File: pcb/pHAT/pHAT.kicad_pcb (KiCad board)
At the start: 2 copper layers, 65 x 30 mm, 37 parts, among them M1 mount1, M2 mount1, M3 mount1, M4 mount1, P2 USB_A, P4 CONN_01X30, SW1 SW_Push, SW2 SW_Push, SW3 SW_Push, U1 ATTINY25/45/85

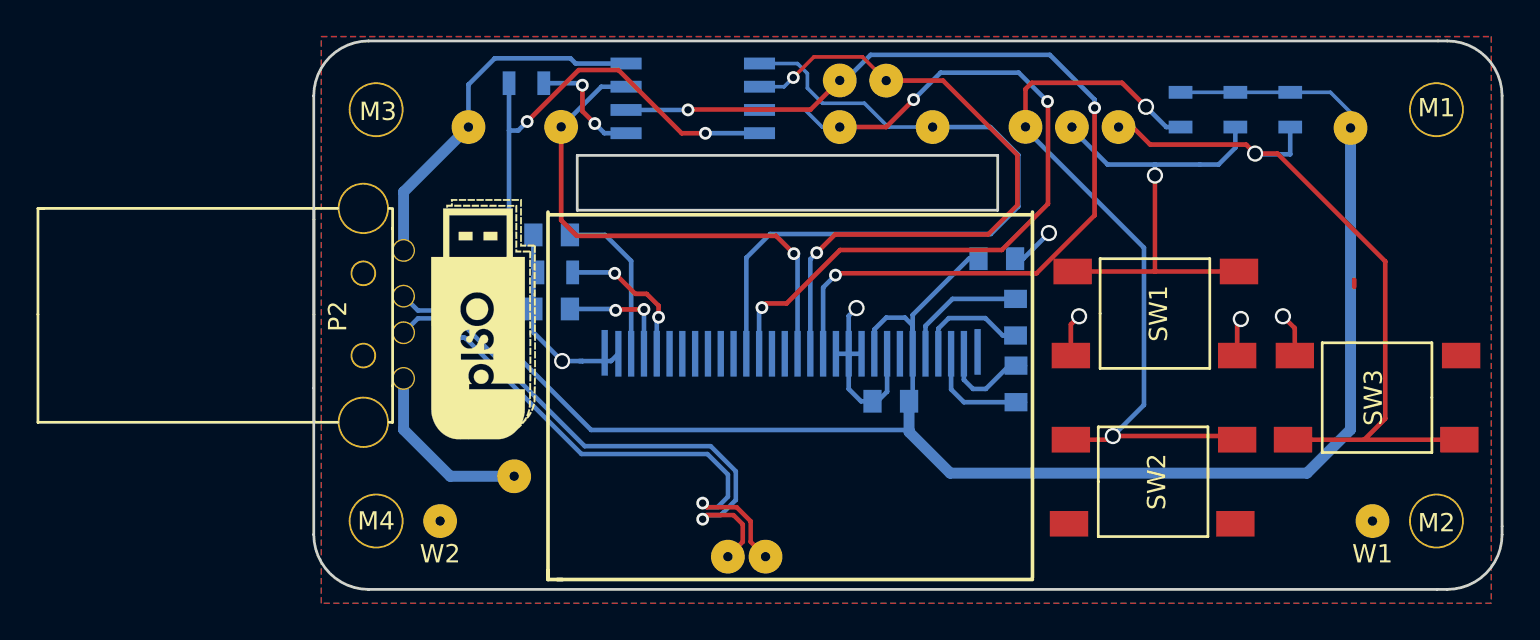
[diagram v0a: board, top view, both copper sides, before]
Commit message: update PCB for 1.2 support
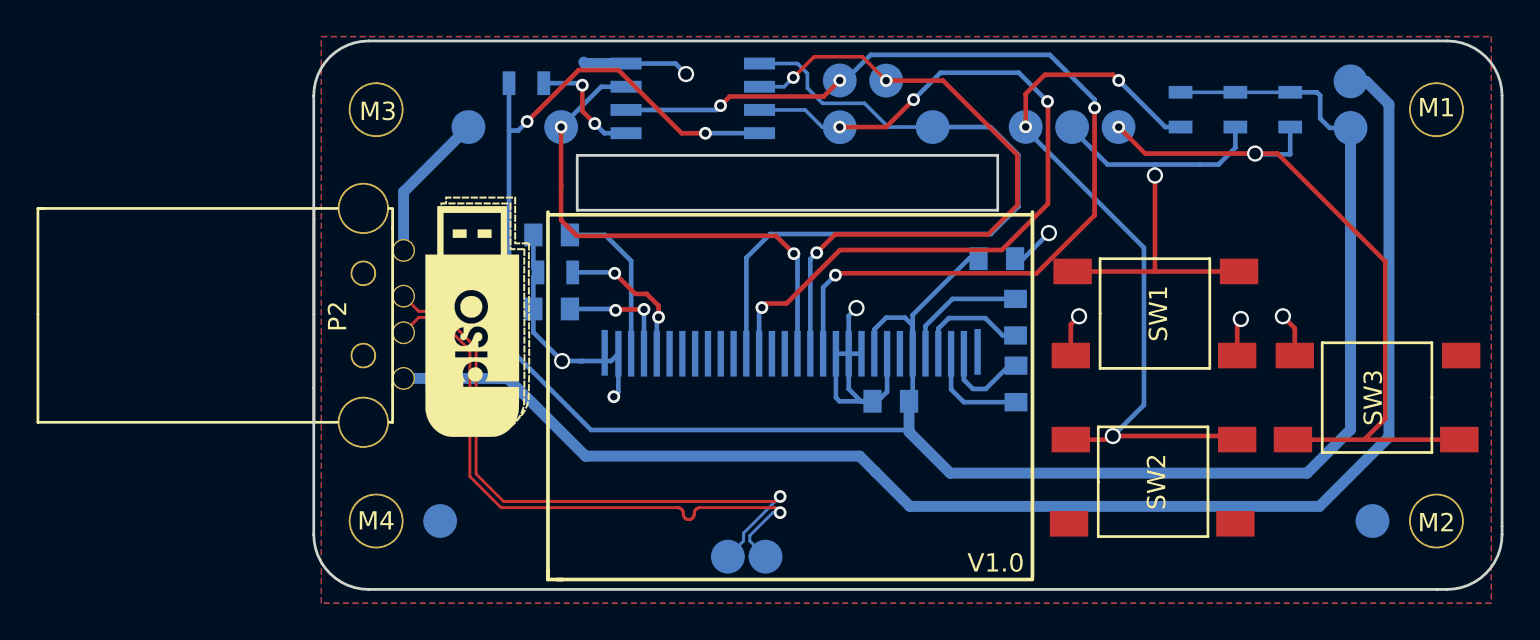
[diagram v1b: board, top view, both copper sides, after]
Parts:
- removed D+: D_P, pISO:SLP
- removed D-: D_N, pISO:SLP
- removed G***: LOGO, pISO:LOGO
- added DNP1: LOGO, pISO:LOGO, F.Cu at (118.5, 94.6)
- added REF***: OSHW-Logo_19x20mm_SilkScreen, Symbols:OSHW-Logo_19x20mm_SilkScreen, B.Cu at (158.7, 95.5)
- added W14: D_N, pISO:SLP, B.Cu at (134.2, 107.7)
- added W15: D_P, pISO:SLP, B.Cu at (132.2, 107.7)
- moved W5 50.6 mm to (166.2, 81.7)
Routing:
- net Net-(P2-Pad1): track 9.91 -> 79.2 mm
- net /DM1_N: track 30.6 -> 34.7 mm
- net /DM1_P: track 30.6 -> 34.7 mm
- net GND: track 52.9 -> 54.1 mm, vias 6 -> 8
- net +3V3: track 124.7 -> 125.8 mm
- net Net-(A1-Pad1): track 42.5 -> 41.7 mm, vias 2 -> 3
- net /CS: vias 3 -> 4
- net /SCLK: vias 3 -> 4
- net /DC: vias 1 -> 2
- net Net-(B1-Pad1): vias 1 -> 2
- net /RST: vias 2 -> 3
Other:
- board text added: "+"
- board text added: "-"
- board text added: "V1.0"

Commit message: update PCB images
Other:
- board text added: "DOWN"
- board text added: "SELECT"
- board text added: "UP"
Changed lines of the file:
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@@
     (area 109.424999 79.424999 174.575001 109.575001)
     (thickness 1.6)
-    (drawings 25)
+    (drawings 28)
     (tracks 333)
     (zones 0)
@@
     (35 F.Paste user)
     (36 B.SilkS user)
-    (37 F.SilkS user hide)
+    (37 F.SilkS user)
     (38 B.Mask user)
     (39 F.Mask user)
@@
   )
   (setup
-    (last_trace_width 0.254)
+    (last_trace_width 0.2)
     (user_trace_width 0.2)
     (user_trace_width 0.25)
@@
   (module pISO:SLP (layer F.Cu)
     (at 167.41188 105.75942)
-    (fp_text reference W1 (at 0.04 5.3) (layer F.SilkS) hide
+    (fp_text reference W1 (at 11.5 -24.5) (layer F.SilkS) hide
       (effects (font (size 1 1) (thickness 0.15)))
     )
@@
   (module pISO:SLP (layer F.Cu)
     (at 116.41188 105.75942)
-    (fp_text reference W2 (at 0.01 5.31) (layer F.SilkS) hide
+    (fp_text reference W2 (at 62.5 -18.5) (layer F.SilkS) hide
       (effects (font (size 1 1) (thickness 0.15)))
     )
@@
   (module pISO:SLP (layer B.Cu)
     (at 134.21188 107.70942)
-    (fp_text reference W14 (at 0.2 3.47) (layer B.SilkS) hide
+    (fp_text reference W14 (at 44.7 -22.45) (layer B.SilkS) hide
       (effects (font (size 1 1) (thickness 0.15)) (justify mirror))
     )
@@
   (module pISO:SLP (layer B.Cu)
     (at 132.15188 107.70942)
-    (fp_text reference W15 (at -0.77 3.65) (layer B.SilkS) hide
+    (fp_text reference W15 (at 46.76 -21.45) (layer B.SilkS) hide
       (effects (font (size 1 1) (thickness 0.15)) (justify mirror))
     )
@@
   (module pISO:SLP (layer B.Cu)
     (at 148.44188 84.19942)
-    (fp_text reference A1 (at 0.13 -5.8) (layer B.SilkS) hide
+    (fp_text reference A1 (at 30.47 0.06) (layer B.SilkS) hide
       (effects (font (size 1 1) (thickness 0.15)) (justify mirror))
     )
@@
   (module pISO:SLP (layer B.Cu)
     (at 153.52188 84.20942)
-    (fp_text reference B1 (at 0.14 -5.71) (layer B.SilkS) hide
+    (fp_text reference B1 (at 25.39 -0.95) (layer B.SilkS) hide
       (effects (font (size 1 1) (thickness 0.15)) (justify mirror))
     )
@@
   (module pISO:SLP (layer B.Cu)
     (at 150.98188 84.20942)
-    (fp_text reference NO1 (at 0.17 -6.2) (layer B.SilkS) hide
+    (fp_text reference NO1 (at 27.93 -1.95) (layer B.SilkS) hide
       (effects (font (size 1 1) (thickness 0.15)) (justify mirror))
     )
@@
   (module pISO:SLP (layer B.Cu)
     (at 166.21188 81.70942)
-    (fp_text reference W5 (at 0.03 -4.9) (layer B.SilkS) hide
+    (fp_text reference W5 (at 12.7 -2.45) (layer B.SilkS) hide
       (effects (font (size 1 1) (thickness 0.15)) (justify mirror))
     )
@@
   (module pISO:SLP (layer B.Cu)
     (at 140.81188 81.66942)
-    (fp_text reference W7 (at 0.01 -5.09) (layer B.SilkS) hide
+    (fp_text reference W7 (at 38.1 7.59) (layer B.SilkS) hide
       (effects (font (size 1 1) (thickness 0.15)) (justify mirror))
     )
@@
   (module pISO:SLP (layer B.Cu)
     (at 138.27188 81.65942)
-    (fp_text reference W8 (at 0.31 -5.52) (layer B.SilkS) hide
+    (fp_text reference W8 (at 40.64 9.6) (layer B.SilkS) hide
       (effects (font (size 1 1) (thickness 0.15)) (justify mirror))
     )
@@
   (module pISO:SLP (layer B.Cu)
     (at 143.35188 84.20942)
-    (fp_text reference W9 (at -0.22 -6.82) (layer B.SilkS) hide
+    (fp_text reference W9 (at 35.56 4.05) (layer B.SilkS) hide
       (effects (font (size 1 1) (thickness 0.15)) (justify mirror))
     )
@@
   (module pISO:SLP (layer B.Cu)
     (at 138.27188 84.21942)
-    (fp_text reference W10 (at 0.17 -6.35) (layer B.SilkS) hide
+    (fp_text reference W10 (at 40.64 6.04) (layer B.SilkS) hide
       (effects (font (size 1 1) (thickness 0.15)) (justify mirror))
     )
@@
   (module pISO:SLP (layer B.Cu)
     (at 123.03188 84.20942)
-    (fp_text reference W11 (at 0 -6.64) (layer B.SilkS) hide
+    (fp_text reference W11 (at 55.88 8.05) (layer B.SilkS) hide
       (effects (font (size 1 1) (thickness 0.15)) (justify mirror))
     )
@@
   (module pISO:SLP (layer B.Cu)
     (at 117.96188 84.20942)
-    (fp_text reference W12 (at 0.33 -6.99) (layer B.SilkS) hide
+    (fp_text reference W12 (at 60.95 9.05) (layer B.SilkS) hide
       (effects (font (size 1 1) (thickness 0.15)) (justify mirror))
     )
@@
   (module pISO:SLP (layer B.Cu)
     (at 166.21188 84.25942)
-    (fp_text reference W13 (at 0.03 -5.69) (layer B.SilkS) hide
+    (fp_text reference W13 (at 12.7 -4) (layer B.SilkS) hide
       (effects (font (size 1 1) (thickness 0.15)) (justify mirror))
     )
@@
       (xy 1.060052 9.972623) (xy 1.248305 8.97404)) (layer B.SilkS) (width 0.01))
   )
+  (gr_text SELECT (at 167.71188 95.25942) (layer F.SilkS)
+    (effects (font (size 1 1) (thickness 0.25)))
+  )
+  (gr_text DOWN (at 155.21188 99.85942) (layer F.SilkS)
+    (effects (font (size 1 1) (thickness 0.25)))
+  )
+  (gr_text UP (at 155.41188 90.65942) (layer F.SilkS)
+    (effects (font (size 1 1) (thickness 0.25)))
+  )
   (gr_text V1.0 (at 146.81188 108.05942) (layer F.SilkS)

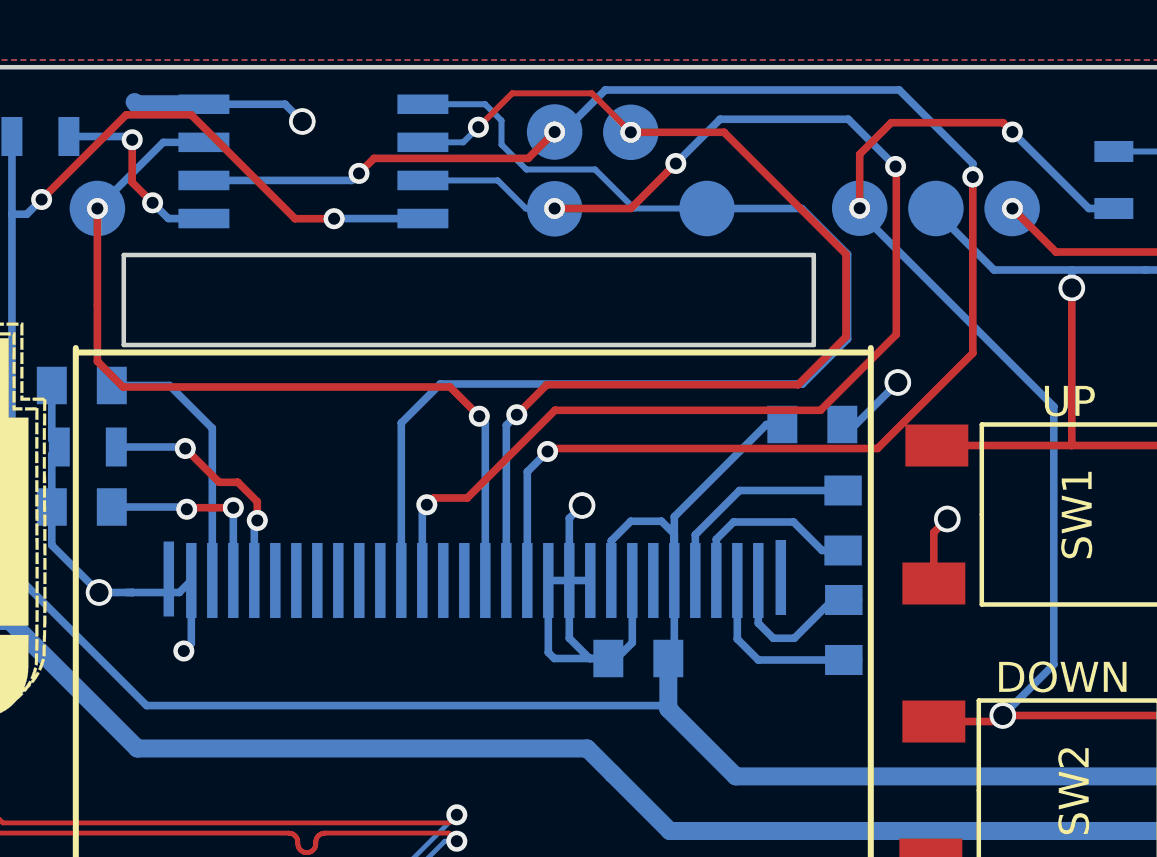
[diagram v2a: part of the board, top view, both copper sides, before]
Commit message: fixed issue that could cause CS line to short to up button
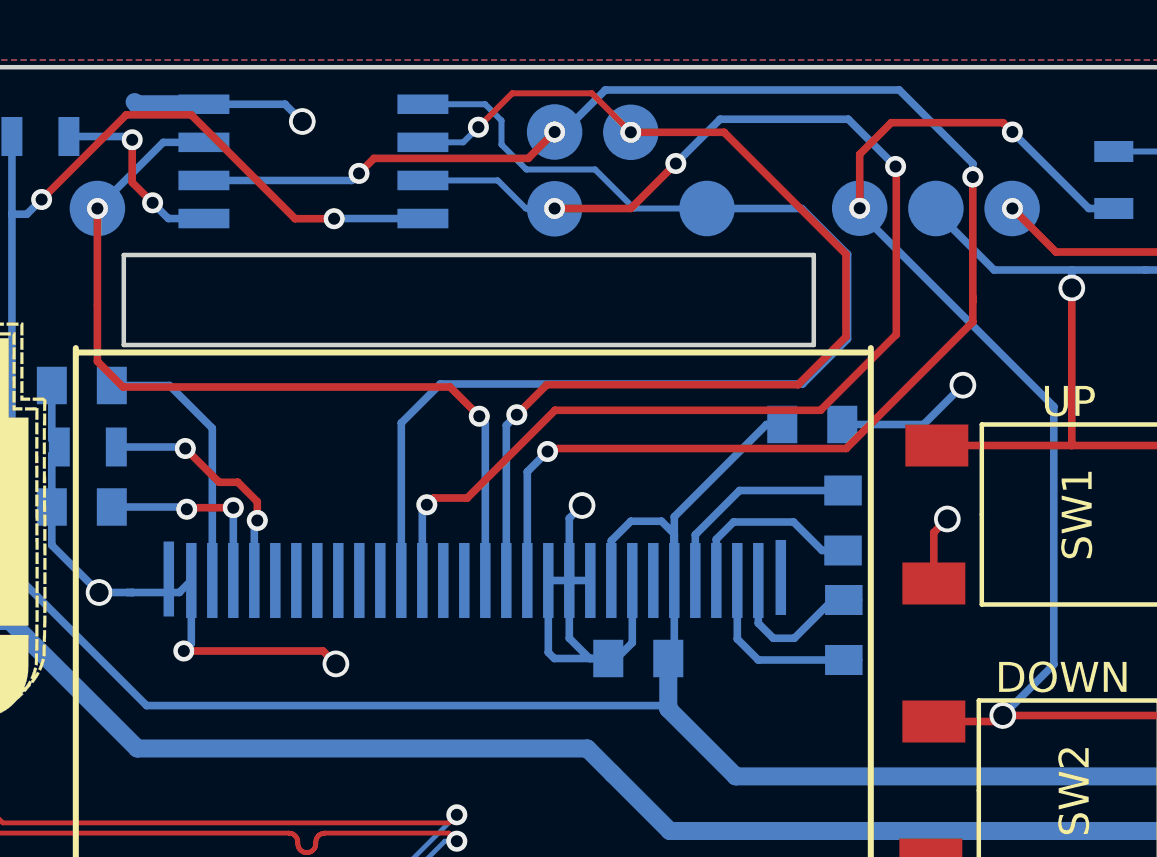
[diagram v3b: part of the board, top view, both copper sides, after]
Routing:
- net GND: track 54.1 -> 60.1 mm, vias 8 -> 9
- net /CS: track 54.3 -> 53.7 mm
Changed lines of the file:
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@@
     (links 65)
     (no_connects 1)
-    (area 109.424999 79.424999 174.575001 109.575001)
+    (area 94.236879 78.08442 180.53569 110.48442)
     (thickness 1.6)
     (drawings 28)
-    (tracks 333)
+    (tracks 338)
     (zones 0)
     (modules 38)
@@
   )
   (setup
-    (last_trace_width 0.2)
+    (last_trace_width 0.254)
     (user_trace_width 0.2)
     (user_trace_width 0.25)
@@
   (gr_arc (start 171.5 82.5) (end 171.5 79.5) (angle 90) (layer Edge.Cuts) (width 0.15))
   (gr_arc (start 112.5 82.5) (end 109.5 82.5) (angle 90) (layer Edge.Cuts) (width 0.15))
+  (segment (start 125.91188 98.95942) (end 130.55188 98.95942) (width 0.254) (layer F.Cu) (net 1))
+  (segment (start 126.16188 98.70942) (end 125.91188 98.95942) (width 0.254) (layer B.Cu) (net 1))
+  (via (at 125.91188 98.95942) (size 0.7) (drill 0.4) (layers F.Cu B.Cu) (net 1))
   (segment (start 126.16188 96.60942) (end 126.16188 98.70942) (width 0.254) (layer B.Cu) (net 1))
-  (via (at 125.91188 98.95942) (size 0.7) (drill 0.4) (layers F.Cu B.Cu) (net 1))
-  (segment (start 126.16188 98.70942) (end 125.91188 98.95942) (width 0.254) (layer B.Cu) (net 1))
+  (via (at 130.98188 99.38942) (size 0.889) (drill 0.635) (layers F.Cu B.Cu) (net 1))
+  (segment (start 130.55188 98.95942) (end 130.98188 99.38942) (width 0.254) (layer F.Cu) (net 1))
+  (segment (start 147.86188 91.40942) (end 150.57188 91.40942) (width 0.254) (layer B.Cu) (net 1) (status 400000))
+  (via (at 151.88188 90.09942) (size 0.889) (drill 0.635) (layers F.Cu B.Cu) (net 1))
+  (segment (start 150.57188 91.40942) (end 151.88188 90.09942) (width 0.254) (layer B.Cu) (net 1))
   (segment (start 138.06188 96.60942) (end 138.06188 99.00942) (width 0.254) (layer B.Cu) (net 1))
   (segment (start 138.26188 99.20942) (end 140.06188 99.20942) (width 0.254) (layer B.Cu) (net 1))
@@
   (segment (start 129.28688 80.73442) (end 129.86188 81.30942) (width 0.254) (layer B.Cu) (net 1))
   (segment (start 147.86188 91.40942) (end 148.31188 91.40942) (width 0.254) (layer B.Cu) (net 1))
-  (segment (start 148.31188 91.40942) (end 149.71188 90.00942) (width 0.254) (layer B.Cu) (net 1))
-  (via (at 149.71188 90.00942) (size 0.889) (drill 0.635) (layers F.Cu B.Cu) (net 1))
   (segment (start 150.91188 96.70942) (end 150.91188 95.00942) (width 0.254) (layer F.Cu) (net 1))
   (via (at 151.36188 94.55942) (size 0.889) (drill 0.635) (layers F.Cu B.Cu) (net 1))
@@
   (segment (start 121.51188 94.15942) (end 121.51188 95.43442) (width 0.254) (layer B.Cu) (net 1))
   (segment (start 121.51188 95.43442) (end 123.08688 97.00942) (width 0.254) (layer B.Cu) (net 1))
-  (segment (start 148.31188 91.40942) (end 149.62188 90.09942) (width 0.2) (layer B.Cu) (net 1))
   (segment (start 121.51188 90.10942) (end 121.51188 91.90942) (width 0.254) (layer B.Cu) (net 1))
   (segment (start 121.51188 91.90942) (end 121.76188 92.15942) (width 0.254) (layer B.Cu) (net 1))
@@
   (segment (start 134.01188 94.08442) (end 133.86188 94.23442) (width 0.254) (layer B.Cu) (net 7))
   (segment (start 133.86188 94.23442) (end 133.86188 96.60942) (width 0.254) (layer B.Cu) (net 7))
+  (segment (start 152.21188 87.29942) (end 152.21188 87.98942) (width 0.254) (layer F.Cu) (net 8))
+  (segment (start 152.21188 87.98942) (end 147.99188 92.20942) (width 0.254) (layer F.Cu) (net 8))
+  (segment (start 152.21188 87.16942) (end 152.21188 87.29942) (width 0.254) (layer F.Cu) (net 8))
   (segment (start 126.58188 83.27442) (end 131.51688 83.27442) (width 0.254) (layer B.Cu) (net 8))
   (via (at 138.27188 81.65942) (size 0.7) (drill 0.4) (layers F.Cu B.Cu) (net 8))
@@
   (segment (start 131.51688 83.27442) (end 131.75188 83.03942) (width 0.254) (layer B.Cu) (net 8))
   (segment (start 138.26188 81.66942) (end 138.27188 81.65942) (width 0.254) (layer B.Cu) (net 8))
-  (segment (start 152.21188 83.15942) (end 152.21188 89.03442) (width 0.254) (layer F.Cu) (net 8))
-  (segment (start 152.21188 89.03442) (end 149.03688 92.20942) (width 0.254) (layer F.Cu) (net 8))
-  (segment (start 149.03688 92.20942) (end 138.13688 92.20942) (width 0.254) (layer F.Cu) (net 8))
+  (segment (start 152.21188 83.15942) (end 152.21188 87.16942) (width 0.254) (layer F.Cu) (net 8))
+  (segment (start 147.99188 92.20942) (end 138.13688 92.20942) (width 0.254) (layer F.Cu) (net 8))
   (segment (start 138.13688 92.20942) (end 138.03688 92.30942) (width 0.254) (layer F.Cu) (net 8))
   (via (at 138.03688 92.30942) (size 0.7) (drill 0.4) (layers F.Cu B.Cu) (net 8))
